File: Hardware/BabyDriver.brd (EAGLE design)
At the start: 78.7 x 53.3 mm, 34 parts, among them U1 L6470

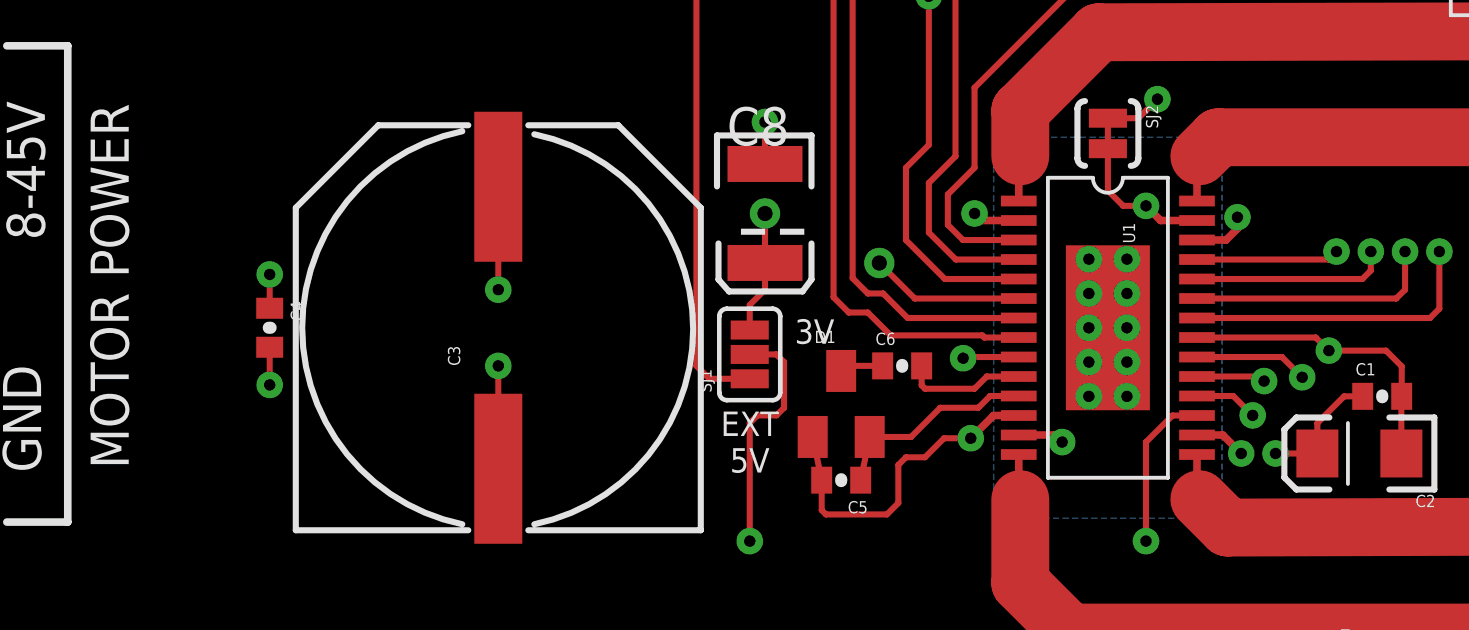
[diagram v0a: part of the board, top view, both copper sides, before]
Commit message: v01 files, as sent to protos.
Mostly unchanged from initial commit; changed some part placements,
some silk.
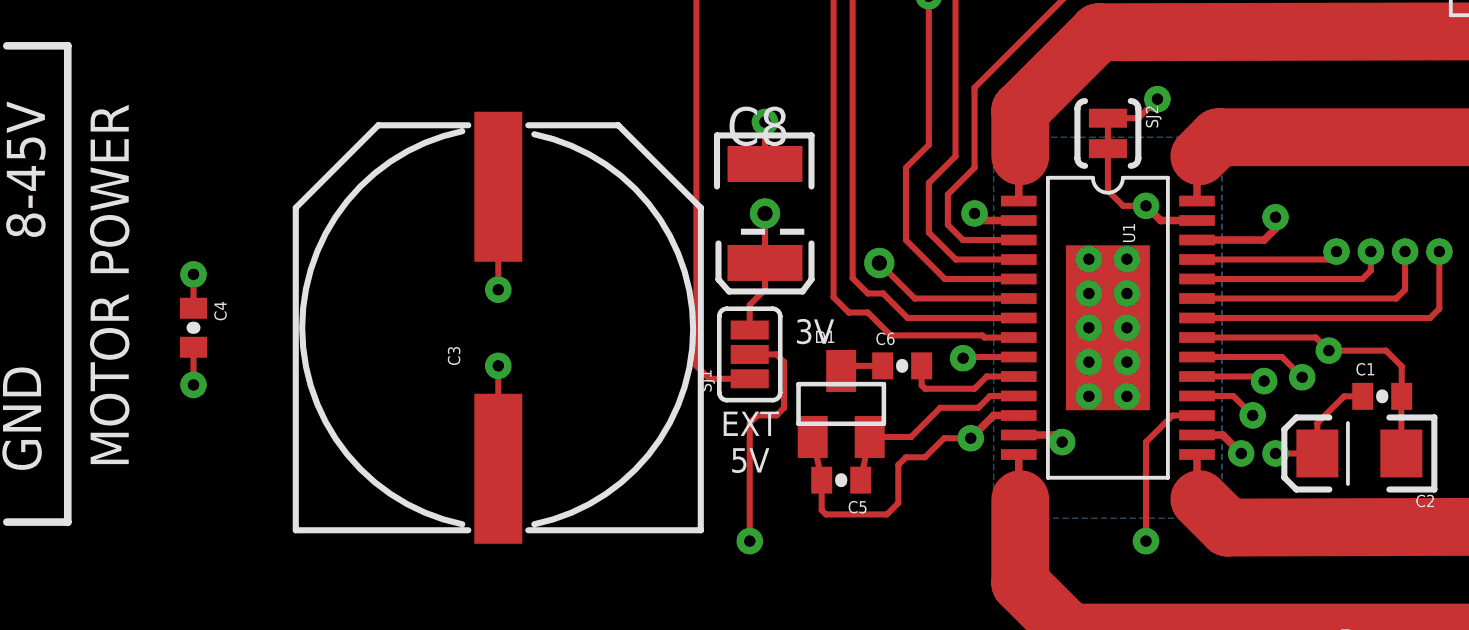
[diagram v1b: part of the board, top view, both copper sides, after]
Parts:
- moved C4 2.54 mm to (14.0, 15.2)
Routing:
- net VS: track 34.9 -> 36.3 mm
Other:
- board text added: "BREADBOARD COMPATIBLE"
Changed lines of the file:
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@@
 <layer number="2" name="Route2" color="1" fill="3" visible="no" active="yes"/>
 <layer number="15" name="Route15" color="4" fill="6" visible="no" active="yes"/>
-<layer number="16" name="Bottom" color="1" fill="1" visible="yes" active="yes"/>
+<layer number="16" name="Bottom" color="1" fill="1" visible="no" active="yes"/>
 <layer number="17" name="Pads" color="2" fill="1" visible="yes" active="yes"/>
 <layer number="18" name="Vias" color="2" fill="1" visible="yes" active="yes"/>
@@
 <layer number="22" name="bPlace" color="14" fill="1" visible="yes" active="yes"/>
 <layer number="23" name="tOrigins" color="15" fill="1" visible="yes" active="yes"/>
-<layer number="24" name="bOrigins" color="15" fill="1" visible="yes" active="yes"/>
+<layer number="24" name="bOrigins" color="15" fill="1" visible="no" active="yes"/>
 <layer number="25" name="tNames" color="7" fill="1" visible="no" active="yes"/>
 <layer number="26" name="bNames" color="7" fill="1" visible="no" active="yes"/>
@@
 <layer number="42" name="bRestrict" color="1" fill="10" visible="no" active="yes"/>
 <layer number="44" name="Drills" color="7" fill="1" visible="no" active="yes"/>
-<layer number="45" name="Holes" color="7" fill="1" visible="yes" active="yes"/>
-<layer number="51" name="tDocu" color="6" fill="1" visible="yes" active="yes"/>
+<layer number="45" name="Holes" color="7" fill="1" visible="no" active="yes"/>
+<layer number="51" name="tDocu" color="6" fill="1" visible="no" active="yes"/>
 <layer number="3" name="Route3" color="4" fill="3" visible="no" active="no"/>
 <layer number="4" name="Route4" color="1" fill="4" visible="no" active="no"/>
@@
 <wire x1="9.779" y1="8.763" x2="7.747" y2="8.763" width="0.254" layer="21"/>
 <text x="11.811" y="10.541" size="1.27" layer="21" font="vector" ratio="15" rot="R90">MOTOR POWER</text>
+<text x="51.181" y="45.847" size="0.8128" layer="22" font="vector" ratio="15" rot="SMR270" align="bottom-right">GND</text>
+<text x="53.721" y="45.847" size="0.8128" layer="22" font="vector" ratio="15" rot="SMR270" align="bottom-right">FLAGN</text>
+<text x="56.261" y="45.847" size="0.8128" layer="22" font="vector" ratio="15" rot="SMR270" align="bottom-right">RESETN</text>
+<text x="68.961" y="45.847" size="0.8128" layer="22" font="vector" ratio="15" rot="SMR270" align="bottom-right">BUSYN</text>
+<text x="71.501" y="45.847" size="0.8128" layer="22" font="vector" ratio="15" rot="SMR270" align="bottom-right">CSN</text>
+<text x="74.041" y="45.847" size="0.8128" layer="22" font="vector" ratio="15" rot="SMR270" align="bottom-right">STCK</text>
+<text x="5.461" y="45.72" size="0.8128" layer="22" font="vector" ratio="15" rot="SMR270" align="bottom-right">GND</text>
+<text x="8.001" y="45.72" size="0.8128" layer="22" font="vector" ratio="15" rot="SMR270" align="bottom-right">OSCOUT</text>
+<text x="10.541" y="45.72" size="0.8128" layer="22" font="vector" ratio="15" rot="SMR270" align="bottom-right">MOSI</text>
+<text x="13.081" y="45.72" size="0.8128" layer="22" font="vector" ratio="15" rot="SMR270" align="bottom-right">MISO</text>
+<text x="15.621" y="45.72" size="0.8128" layer="22" font="vector" ratio="15" rot="SMR270" align="bottom-right">3-5V</text>
+<text x="28.321" y="45.72" size="0.8128" layer="22" font="vector" ratio="15" rot="SMR270" align="bottom-right">GND</text>
+<text x="30.861" y="45.72" size="0.8128" layer="22" font="vector" ratio="15" rot="SMR270" align="bottom-right">OSCOUT</text>
+<text x="33.401" y="45.72" size="0.8128" layer="22" font="vector" ratio="15" rot="SMR270" align="bottom-right">SCK</text>
+<text x="35.941" y="45.72" size="0.8128" layer="22" font="vector" ratio="15" rot="SMR270" align="bottom-right">OSCIN</text>
+<text x="38.481" y="45.72" size="0.8128" layer="22" font="vector" ratio="15" rot="SMR270" align="bottom-right">3-5V</text>
+<wire x1="3.81" y1="45.72" x2="3.81" y2="43.18" width="0.254" layer="22"/>
+<wire x1="3.81" y1="43.18" x2="74.93" y2="43.18" width="0.254" layer="22"/>
+<wire x1="74.93" y1="43.18" x2="74.93" y2="45.72" width="0.254" layer="22"/>
+<text x="50.165" y="49.149" size="1.27" layer="22" font="vector" ratio="15" rot="MR0">BREADBOARD
+COMPATIBLE</text>
 </plain>
 <attributes>
@@
 <attribute name="VALUE" value="10nF" x="35.56" y="10.16" size="1.778" layer="27" rot="R180" display="off"/>
 </element>
-<element name="C4" library="SparkFun-Capacitors" package="0402-CAP" value="0.22uF" x="16.51" y="15.24" rot="R270">
-<attribute name="PROD_ID" value="CAP-09885" x="16.51" y="15.24" size="1.778" layer="27" rot="R270" display="off"/>
-<attribute name="VALUE" value=".22uF" x="16.51" y="15.24" size="1.778" layer="27" rot="R270" display="off"/>
+<element name="C4" library="SparkFun-Capacitors" package="0402-CAP" value="0.22uF" x="13.97" y="15.24" rot="R270">
+<attribute name="PROD_ID" value="CAP-09885" x="13.97" y="15.24" size="1.778" layer="27" rot="R270" display="off"/>
+<attribute name="VALUE" value=".22uF" x="13.97" y="15.24" size="1.778" layer="27" rot="R270" display="off"/>
 </element>
 <element name="C3" library="SparkFun-Capacitors" package="PANASONIC_H13" value="100uF" x="24.13" y="15.24" rot="R90">
@@
 <contactref element="JP6" pad="1"/>
 <contactref element="JP6" pad="2"/>
-<wire x1="47.42" y1="18.165" x2="48.391" y2="18.165" width="0.254" layer="1"/>
-<wire x1="48.391" y1="18.165" x2="48.768" y2="18.542" width="0.254" layer="1"/>
-<wire x1="48.768" y1="18.542" x2="48.768" y2="18.923" width="0.254" layer="1"/>
-<via x="48.768" y="18.923" extent="1-16" drill="0.381"/>
+<wire x1="47.42" y1="18.165" x2="49.661" y2="18.165" width="0.254" layer="1"/>
+<wire x1="49.661" y1="18.165" x2="50.038" y2="18.542" width="0.254" layer="1"/>
+<wire x1="50.038" y1="18.542" x2="50.038" y2="18.923" width="0.254" layer="1"/>
+<via x="50.038" y="18.923" extent="1-16" drill="0.381"/>
 <wire x1="41.48" y1="18.815" x2="40.24" y2="18.815" width="0.254" layer="1"/>
 <wire x1="40.24" y1="18.815" x2="40.005" y2="19.05" width="0.254" layer="1"/>
@@
 <wire x1="49.149" y1="27.94" x2="48.768" y2="27.559" width="0.2032" layer="1"/>
 <via x="48.768" y="27.559" extent="1-16" drill="0.381"/>
-<wire x1="48.768" y1="27.559" x2="48.768" y2="18.923" width="0.2032" layer="2"/>
+<wire x1="48.768" y1="27.559" x2="50.038" y2="18.923" width="0.2032" layer="2"/>
 <wire x1="34.61" y1="11.6" x2="34.91" y2="10.16" width="0.2032" layer="1"/>
 <wire x1="34.91" y1="10.16" x2="34.91" y2="9.159" width="0.2032" layer="1"/>
@@
 <wire x1="24.13" y1="19.94" x2="24.13" y2="16.51" width="0.2032" layer="1"/>
 <via x="24.13" y="16.51" extent="1-16" drill="0.381"/>
-<wire x1="16.51" y1="15.89" x2="16.51" y2="17.018" width="0.2032" layer="1"/>
-<via x="16.51" y="17.018" extent="1-16" drill="0.381"/>
+<wire x1="13.97" y1="15.89" x2="13.97" y2="17.018" width="0.2032" layer="1"/>
+<via x="13.97" y="17.018" extent="1-16" drill="0.381"/>
 </signal>
 <signal name="PGND">
@@
 <via x="43.815" y="17.526" extent="1-16" drill="0.381"/>
 <wire x1="44.45" y1="15.24" x2="45.085" y2="15.24" width="0.2032" layer="1"/>
-<wire x1="16.51" y1="14.59" x2="16.51" y2="13.335" width="0.2032" layer="1"/>
-<via x="16.51" y="13.335" extent="1-16" drill="0.381"/>
+<wire x1="13.97" y1="14.59" x2="13.97" y2="13.335" width="0.2032" layer="1"/>
+<via x="13.97" y="13.335" extent="1-16" drill="0.381"/>
 <wire x1="24.13" y1="10.54" x2="24.13" y2="13.97" width="0.2032" layer="1"/>
 <via x="24.13" y="13.97" extent="1-16" drill="0.381"/>

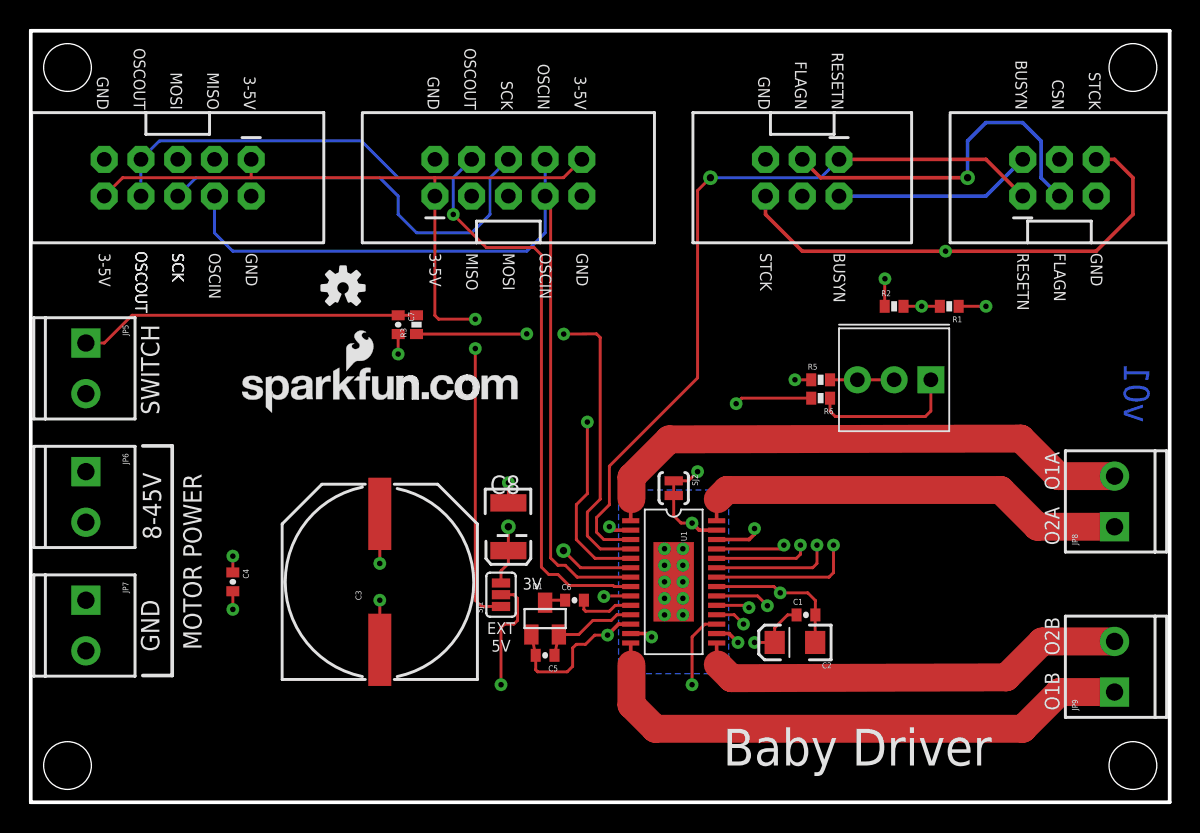
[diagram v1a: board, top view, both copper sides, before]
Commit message: Tidying up the example code some; that's still in process.
This is to update the hardware files to v02- shrink the board
a bit.
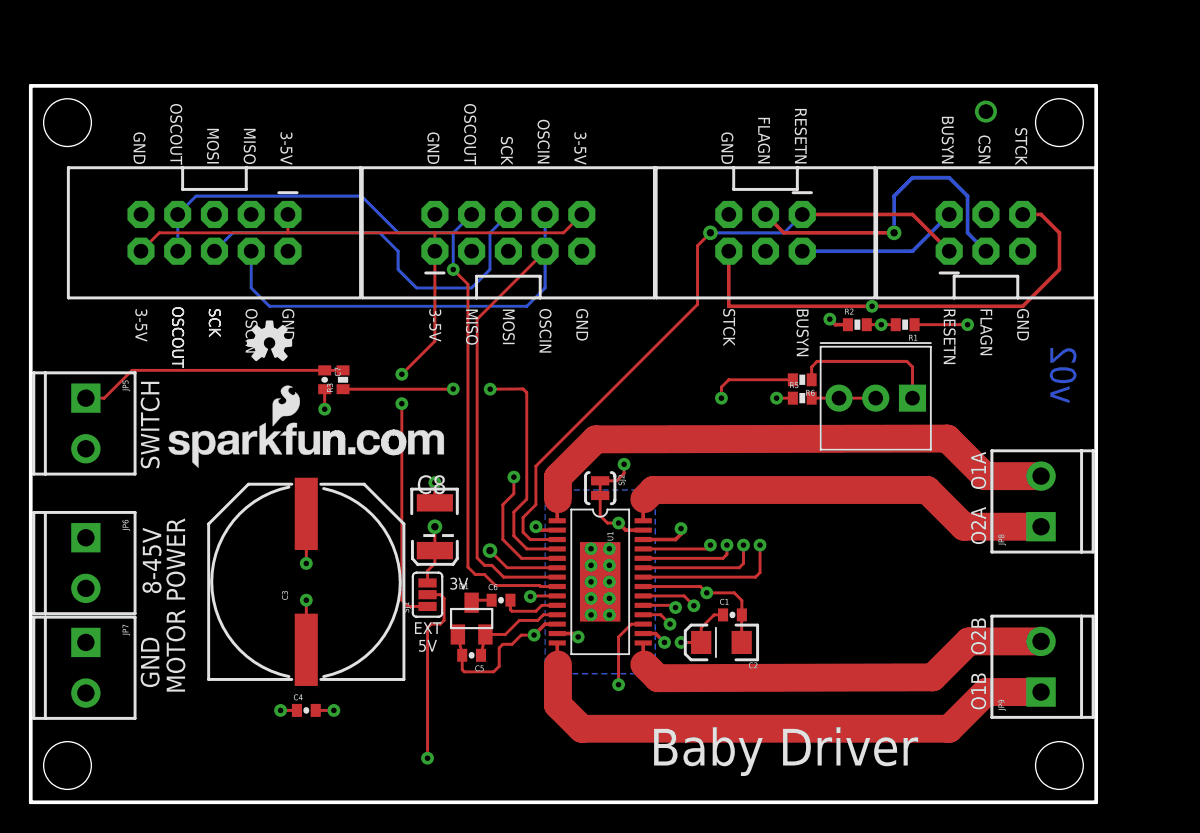
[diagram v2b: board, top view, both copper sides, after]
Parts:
- moved C4 10.2 mm to (19.1, 6.35), turned to 0 degrees
- moved R3 6.35 mm to (21.6, 29.2)
- moved C7 6.35 mm to (20.3, 29.2)
- moved JP4 6.35 mm to (66.0, 39.4)
- moved LOGO1 6.35 mm to (16.5, 31.8)
- moved LOGO2 6.35 mm to (9.53, 23.1)
- moved STANDOFF1 6.35 mm to (71.1, 47.0)
- moved JP8 5.08 mm to (69.8, 19.1)
- moved JP9 5.08 mm to (69.8, 7.62)
- moved SJ2 5.08 mm to (39.4, 21.7)
- moved U1 5.08 mm to (39.4, 15.2)
- moved C5 5.08 mm to (30.5, 10.2)
- moved C8 5.08 mm to (27.9, 19.1)
- moved D1 5.08 mm to (30.5, 12.7)
- moved SJ1 5.08 mm to (27.4, 14.4)
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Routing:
- net VLOGIC: track 75.1 -> 91.3 mm
- net MISO: track 73.6 -> 62.0 mm
- net OSCOUT: track 65.6 -> 55.2 mm
- net MOSI: track 86.9 -> 77.4 mm
- net SCK: track 97.1 -> 87.7 mm
- net N$5: track 34.6 -> 26.5 mm
- net 5V: track 69.2 -> 61.1 mm
- net RESETN: track 53.5 -> 46.7 mm
- net N$6: track 23.7 -> 18.6 mm
- net CSN: track 53.1 -> 58.2 mm, vias 1 -> 2
- net OSCIN: track 62.8 -> 58.2 mm
- net FLAGN: track 78.2 -> 74.2 mm
- net ADC: track 40.0 -> 42.3 mm
- net STCK: track 71.0 -> 73.2 mm
- net VS: track 36.3 -> 38.4 mm
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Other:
- board size 78.7 x 53.3 mm -> 73.7 x 49.5 mm
- board text added: "M.Hord"
- board text added: "v02"
- board text removed: "v01"
